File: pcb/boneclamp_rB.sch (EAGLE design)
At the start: 109 parts, among them IC1 24C, U1 AD8032ARZ-REEL7, U10 ADA4841-2YRZ, U11 ADA4841-2YRZ, U2 LT1964ES5-5TRMPBF, U3 ADA4841-2YRZ, U4 TLV70245DBVT, U6 AD713JRZ-16, U7 AD7682BCPZ, U8 TPS63700DRCT, U9 ADA4841-2YRZ

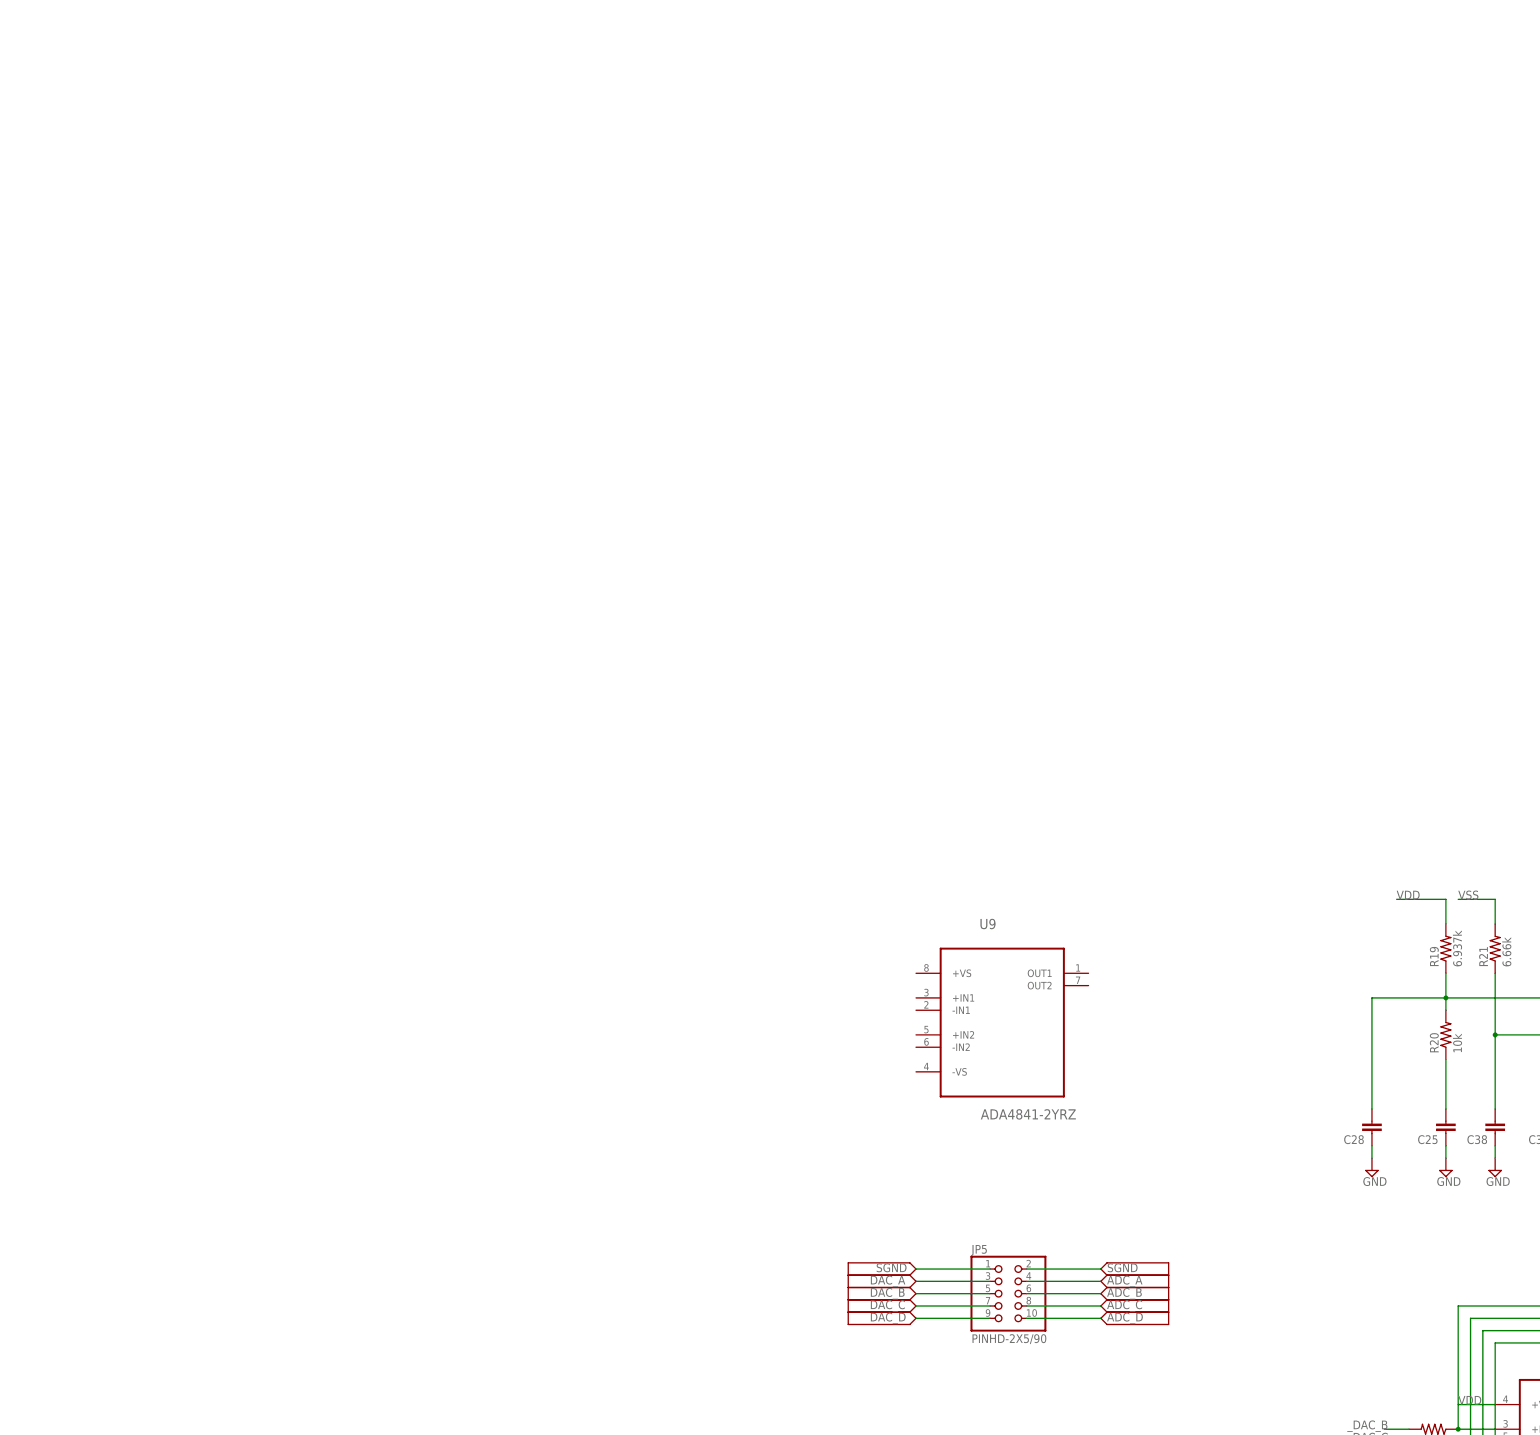
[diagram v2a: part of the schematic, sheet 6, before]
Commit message: Fixed the input biasing scheme. The op-amps we are using require -0.25 to 5.2 volt supply range to push the inputs into the 0 to 4.096 range required by the ADC. This means that our positive rail is too low. We need a boost conveter for the positive rail before the LDO.
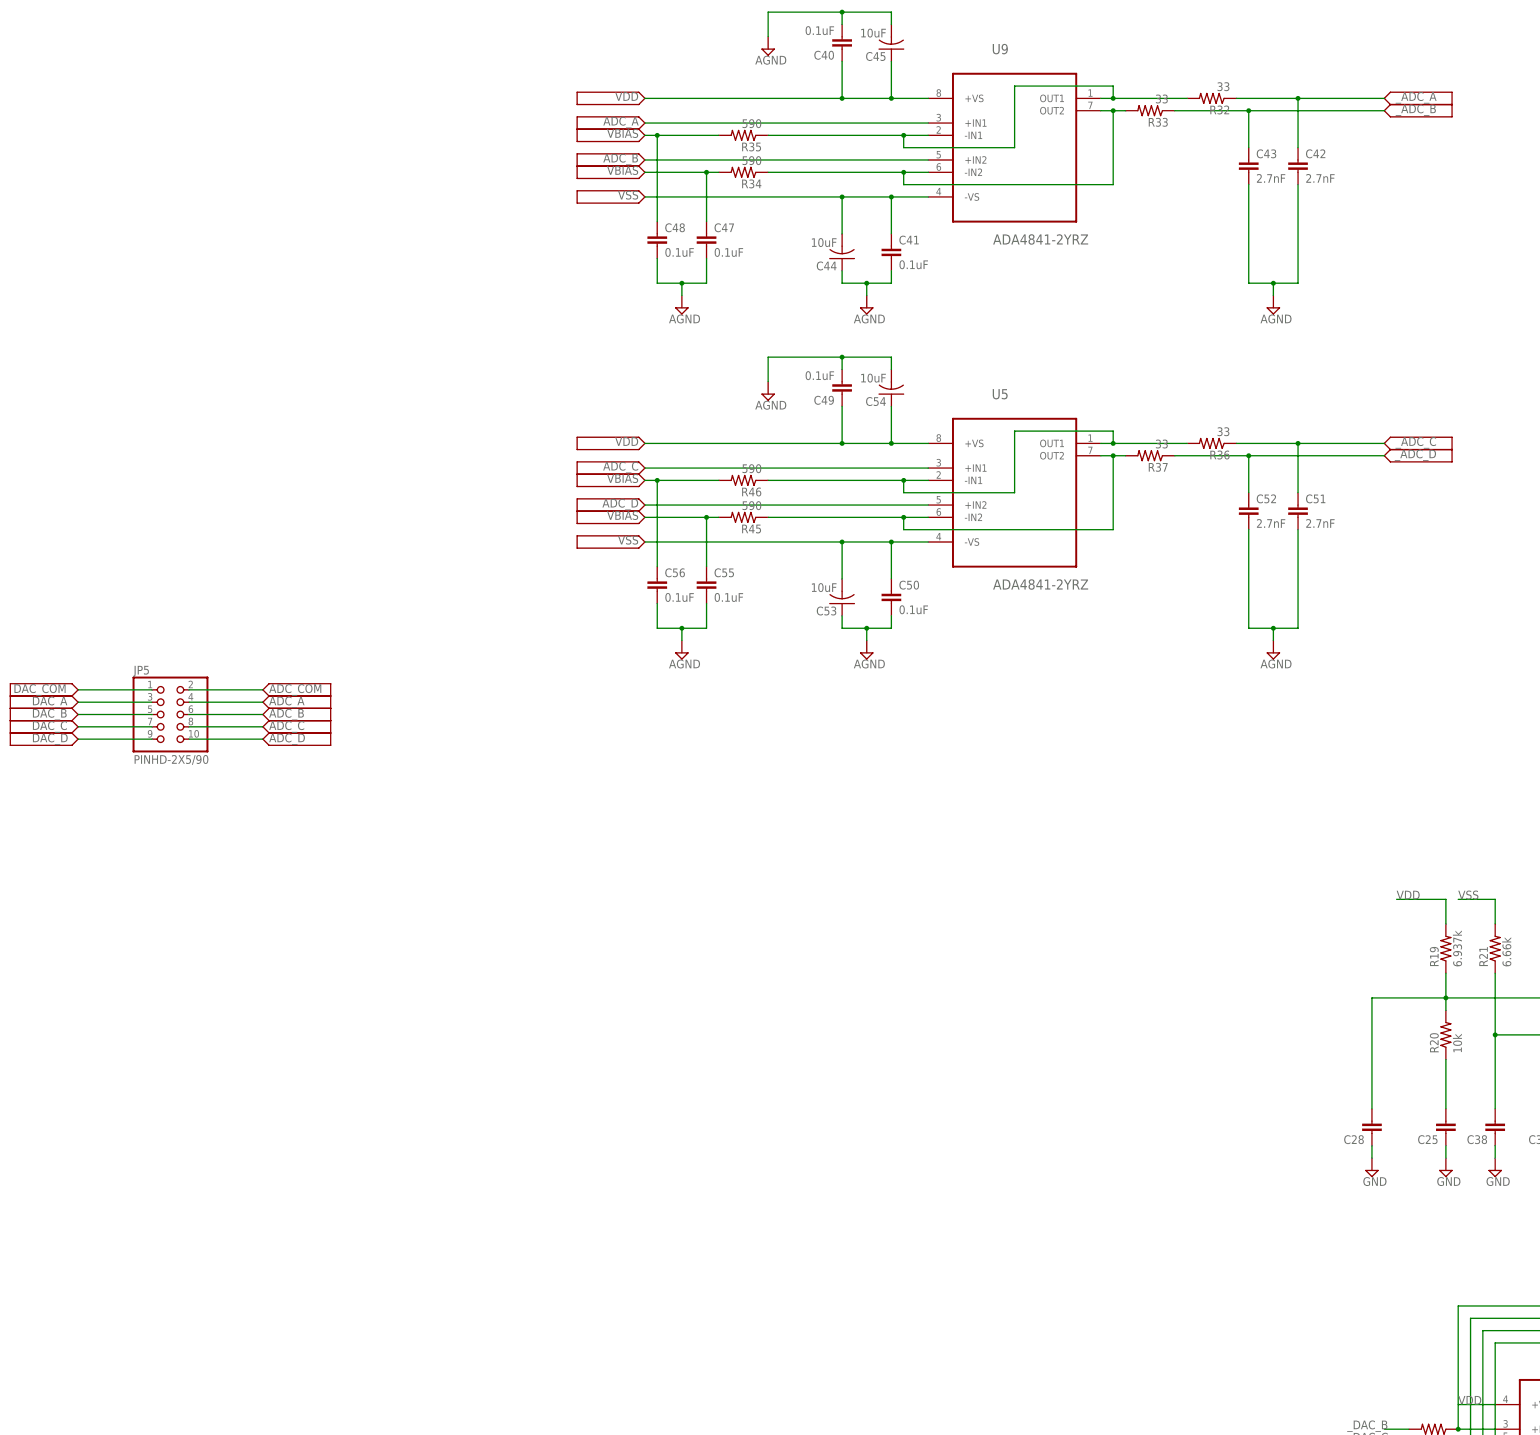
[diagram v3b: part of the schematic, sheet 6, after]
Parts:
- added C40, C41, C46, C47, C48, C49, C50, C55, C56: 0.1uF, rcl:C-EUC0805
- added C42, C43, C51, C52: 2.7nF, rcl:C-EUC0805
- added C44, C45, C53, C54: 10uF, rcl:C-USC0805
- added R32, R33, R36, R37: 33, rcl:R-US_R0603
- added R34, R35, R45, R46: 590, rcl:R-US_R0603
- added U5: ADA4841-2YRZ, analog-devices-01:ADA4841-2YRZ
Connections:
- removed net SGND: JP5.1, JP5.2
- new net ADC_COM: JP5.2
- new net DAC_COM: JP5.1
- new net N$1: R37.2, R45.1, U5.-IN2, U5.OUT2
- new net N$2: R33.2, R34.1, U9.-IN2, U9.OUT2
- new net N$20: R32.2, R35.1, U9.-IN1, U9.OUT1
- new net N$5: R36.2, R46.1, U5.-IN1, U5.OUT1
- new net VBIAS: C46.1, C47.1, C48.1, C55.1, C56.1, R34.2, R35.2, R45.2, R46.2, U1.-IN2, U1.OUT2
- net ADC_A: now also U9.+IN1
- net ADC_B: now also U9.+IN2
- net ADC_C: now also U5.+IN1
- net ADC_D: now also U5.+IN2
- net AGND: now also C40.2, C41.2, C42.2, C43.2, C44.1, C45.2, C46.2, C47.2, C48.2, C49.2, C50.2, C51.2, C52.2, C53.1, C54.2, C55.2, C56.2
- net VCOM: no longer U1.-IN2, U1.OUT2
- net VDD: now also C40.1, C45.1, C49.1, C54.1, U5.+VS, U9.+VS
- net VSS: now also C41.1, C44.2, C50.1, C53.2, U5.-VS, U9.-VS
- net _ADC_A: now also C42.1, R32.1
- net _ADC_B: now also C43.1, R33.1
- net _ADC_C: now also C51.1, R36.1
- net _ADC_D: now also C52.1, R37.1
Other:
- moved on the sheet: JP5, U9

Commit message: I found a potentially better option for the ADC. It is a 100KSPS Serial sampling device from TI. It accepts true bipolar signals of +-VREF using a single supply. It also has as a more resonable SMD package.
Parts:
- added U$77: ADS8343, ti-extended:ADS8343
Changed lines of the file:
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@@
 <setting verticaltext="up"/>
 </settings>
-<grid distance="0.1" unitdist="inch" unit="inch" style="lines" multiple="1" display="yes" altdistance="0.01" altunitdist="inch" altunit="inch"/>
+<grid distance="0.1" unitdist="inch" unit="inch" style="lines" multiple="1" display="no" altdistance="0.01" altunitdist="inch" altunit="inch"/>
 <layers>
 <layer number="1" name="Top" color="4" fill="1" visible="no" active="no"/>
@@
 <part name="SUPPLY32" library="supply2" deviceset="AGND" device=""/>
 <part name="SUPPLY33" library="supply2" deviceset="AGND" device=""/>
+<part name="U$77" library="ti-extended" deviceset="ADS8343" device=""/>
+<part name="U$78" library="boneclamp" deviceset="V_SIG" device=""/>
+<part name="U$79" library="boneclamp" deviceset="V_SIG" device=""/>
+<part name="U$80" library="boneclamp" deviceset="V_SIG" device=""/>
+<part name="U$81" library="boneclamp" deviceset="V_SIG" device=""/>
 </parts>
 <sheets>
@@
 </segment>
 </net>
+</nets>
+</sheet>
+<sheet>
+<description>ALT ADC</description>
+<plain>
+</plain>
+<instances>
+<instance part="U$77" gate="G$1" x="0" y="0"/>
+<instance part="U$78" gate="G$1" x="-27.94" y="12.7" rot="MR0"/>
+<instance part="U$79" gate="G$1" x="-27.94" y="10.16" rot="MR0"/>
+<instance part="U$80" gate="G$1" x="-27.94" y="7.62" rot="MR0"/>
+<instance part="U$81" gate="G$1" x="-27.94" y="5.08" rot="MR0"/>
+</instances>
+<busses>
+</busses>
+<nets>
+<net name="_ADC_A" class="0">
+<segment>
+<wire x1="-27.94" y1="12.7" x2="-12.7" y2="12.7" width="0.1524" layer="91"/>
+<label x="-29.21" y="12.065" size="1.778" layer="95" rot="MR0"/>
+</segment>
+</net>
+<net name="_ADC_B" class="0">
+<segment>
+<wire x1="-12.7" y1="10.16" x2="-27.94" y2="10.16" width="0.1524" layer="91"/>
+<label x="-29.21" y="9.525" size="1.778" layer="95" rot="MR0"/>
+</segment>
+</net>
+<net name="_ADC_C" class="0">
+<segment>
+<wire x1="-27.94" y1="7.62" x2="-12.7" y2="7.62" width="0.1524" layer="91"/>
+<label x="-29.21" y="6.985" size="1.778" layer="95" rot="MR0"/>
+</segment>
+</net>
+<net name="_ADC_D" class="0">
+<segment>
+<wire x1="-12.7" y1="5.08" x2="-27.94" y2="5.08" width="0.1524" layer="91"/>
+<label x="-29.21" y="4.445" size="1.778" layer="95" rot="MR0"/>
+</segment>
+</net>

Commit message: Added the 8331 to schematic. I'm pretty sure this is the right ADC.
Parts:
- removed U$77: ADS8343, ti-extended:ADS8343
